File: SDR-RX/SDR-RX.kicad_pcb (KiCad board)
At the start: 2 copper layers, 43 parts, among them J1 Program, J2 Conn_01x02_Female, J3 Conn_Coaxial, J4 Conn_Coaxial, J5 Conn_01x03_Male, Q1 S8050, Q2 S8050, SW1 Reset ESP, U1 Si4734-D60-GU, U2 ESP32-WROOM-32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

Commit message: changed J2 footprint
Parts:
- J2: footprint Connector_JST:JST_XH_S2B-XH-A_1x02_P2.50mm_Horizontal -> Connector_JST:JST_XH_S2B-XH-A-1_1x02_P2.50mm_Horizontal
- moved C5 6.35 mm to (52.1, -66.0)
- moved TP1 2.54 mm to (94.0, -48.3)
- moved D4 2.54 mm to (59.7, -74.9)
- moved U3 2.54 mm to (52.1, -74.9)
- moved TP4 1.27 mm to (66.0, -48.3)
- moved C12 1.27 mm to (55.9, -66.0)
- moved C6 1.27 mm to (48.3, -66.0)
- moved SW1 1.27 mm to (94.0, -38.1)
- moved J2 1.27 mm to (50.8, -38.1)
- moved TP3 1.27 mm to (81.3, -48.3)

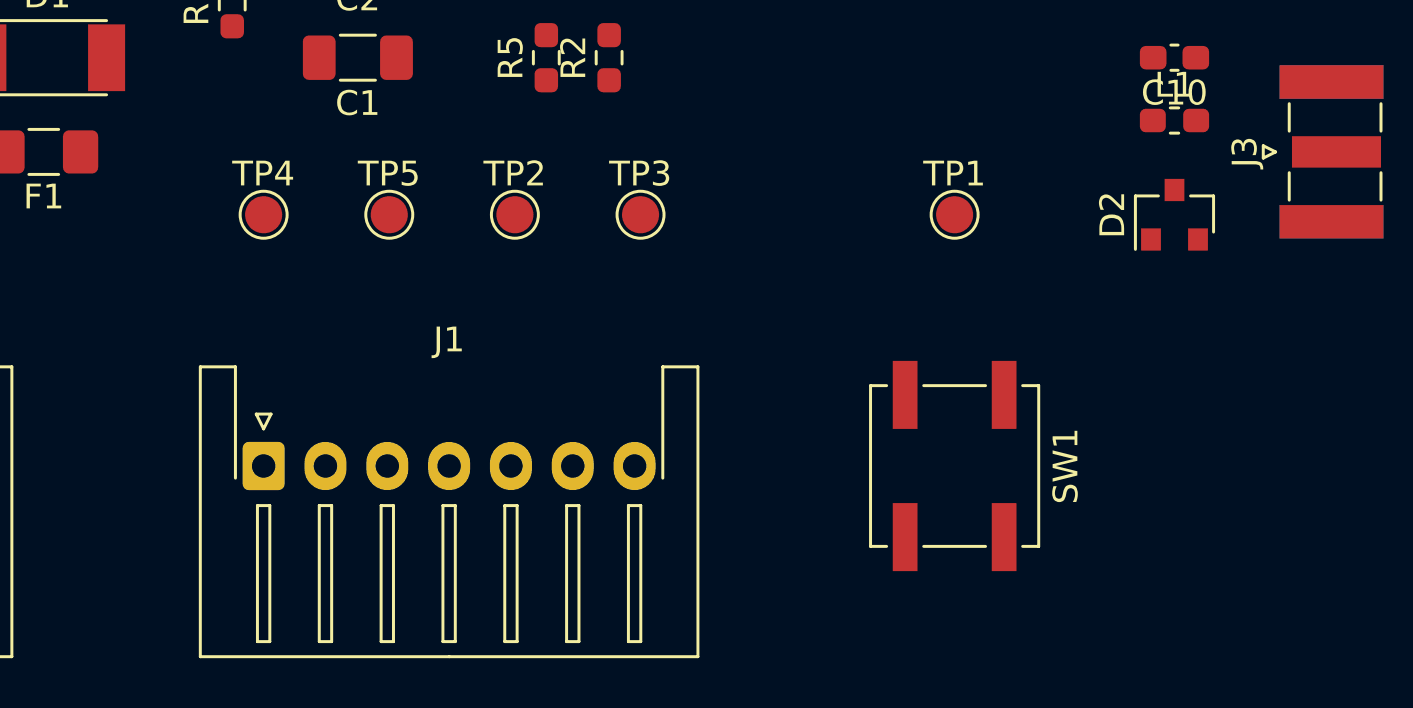
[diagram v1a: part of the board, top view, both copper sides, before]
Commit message: added SW2
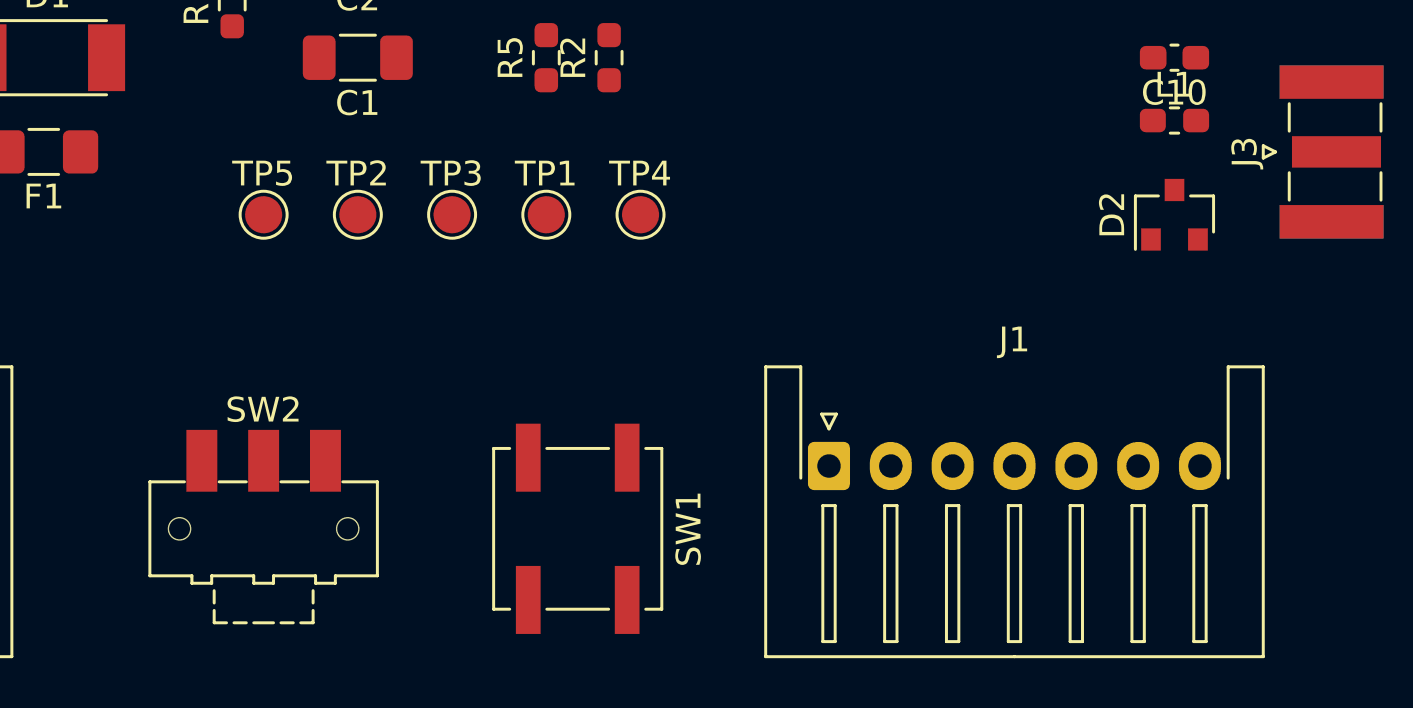
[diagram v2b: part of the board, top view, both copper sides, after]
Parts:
- added SW2: 3V3 J5/J2, Button_Switch_SMD:SW_SPDT_CK-JS102011SAQN, F.Cu at (66.0, -35.6)
- moved J1 22.9 mm to (88.9, -38.1)
- moved TP1 16.5 mm to (77.5, -48.3)
- moved SW1 15.5 mm to (78.7, -35.6)
- moved TP4 15.2 mm to (81.3, -48.3)
- moved TP3 7.62 mm to (73.7, -48.3)
- moved TP2 6.35 mm to (69.8, -48.3)
- moved TP5 5.08 mm to (66.0, -48.3)
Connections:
- C5 pad 1: +3V3 -> Net-(C5-Pad1)
- C6 pad 1: +3V3 -> Net-(C5-Pad1)
- D4 pad 2: +3V3 -> Net-(D4-Pad2)
- J1 pad 5: +3V3 -> Net-(C5-Pad1)
- U3 pad 2: +3V3 -> Net-(D4-Pad2)

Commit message: rearanged parts
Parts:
- moved Y1 14.8 mm to (92.7, -62.2)
- moved C3 14.8 mm to (87.6, -73.7)
- moved C7 14.8 mm to (97.8, -62.2), turned to 0 degrees
- moved C8 14.8 mm to (87.6, -63.5)
- moved C9 14.8 mm to (87.6, -68.6)
- moved U1 14.8 mm to (95.2, -69.8)
- moved C4 14.8 mm to (87.6, -66.0)
- moved R6 14.8 mm to (87.6, -71.1)
- moved C10 12.8 mm to (104.1, -67.3)
- moved C11 12.8 mm to (104.1, -81.3)
- moved D2 12.8 mm to (104.1, -61.0)
- moved D3 12.8 mm to (104.1, -77.5)
- moved J3 12.8 mm to (110.5, -63.5)
- moved L1 12.8 mm to (104.1, -64.8)
- moved J4 12.8 mm to (110.5, -78.7)
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
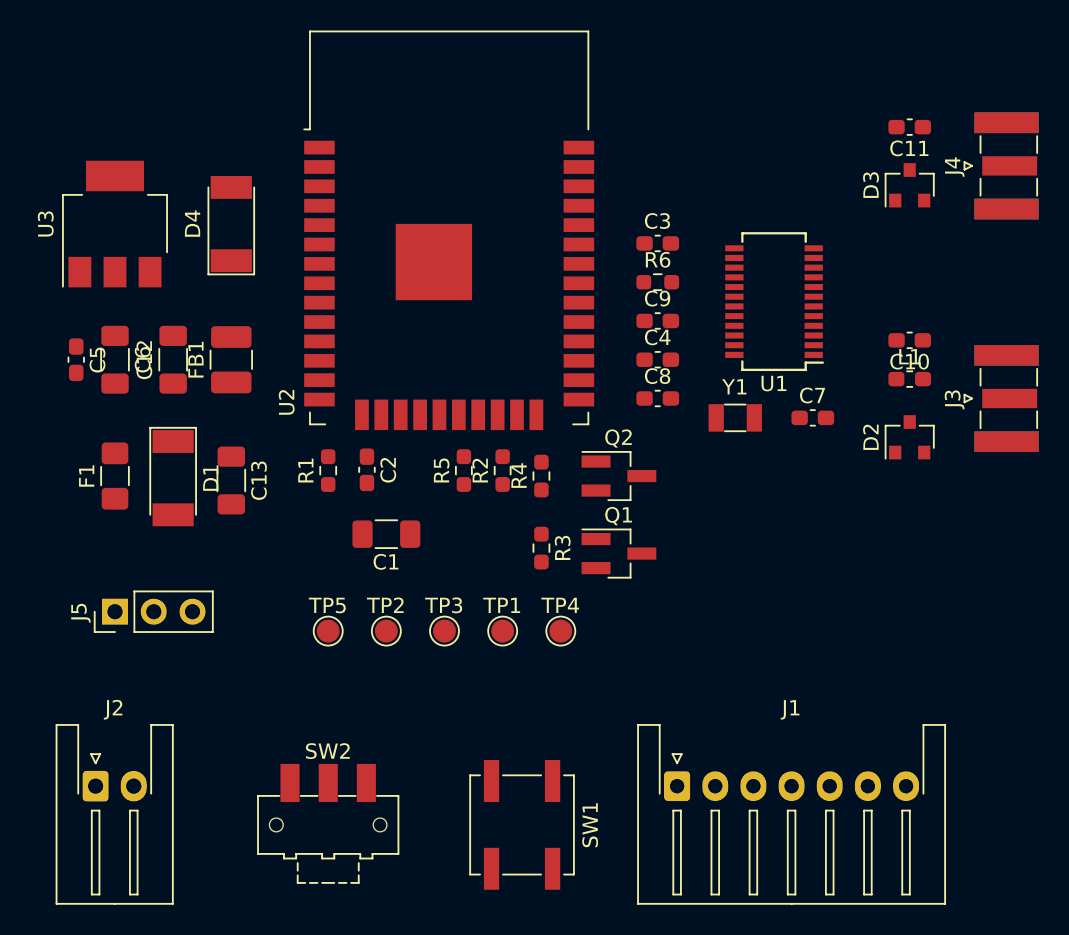
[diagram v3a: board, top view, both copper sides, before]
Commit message: put parts closer on PCB
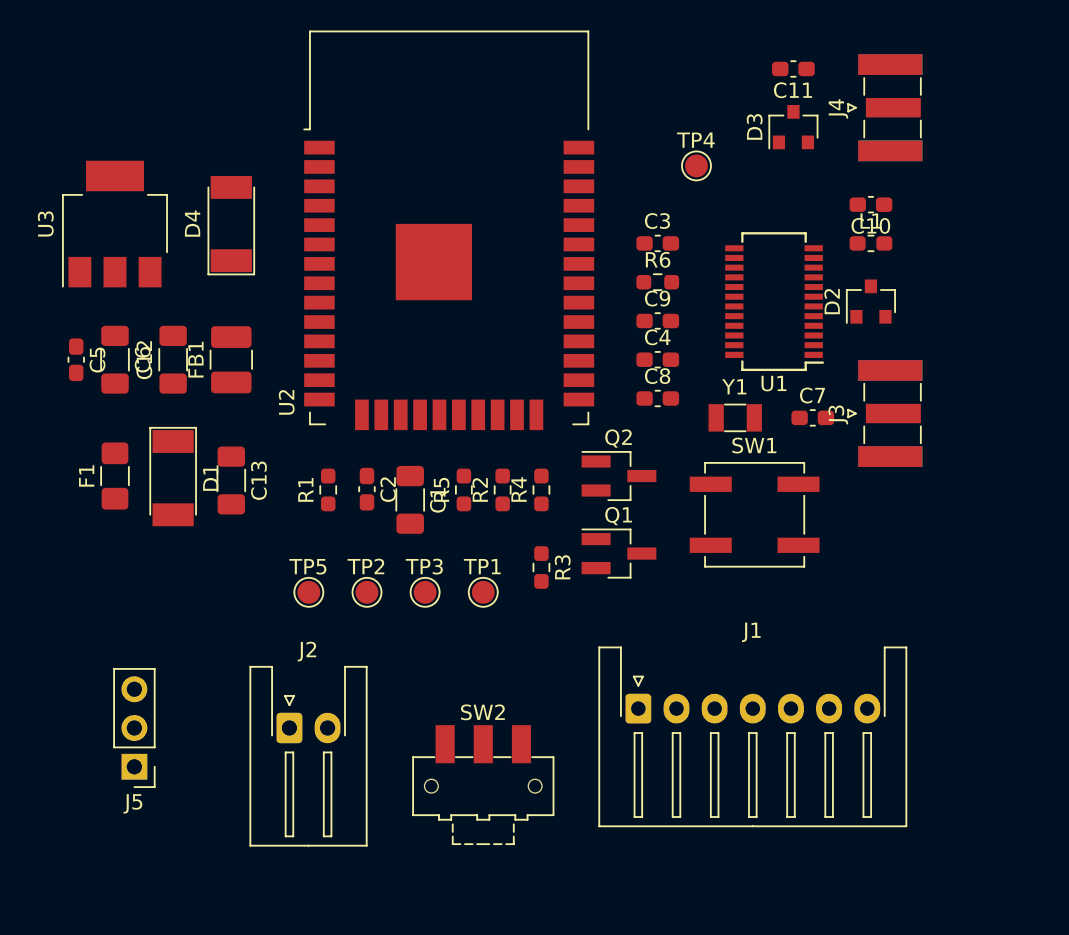
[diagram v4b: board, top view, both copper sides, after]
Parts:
- FB1: value 0Ω @ 100MHZ 1A -> 1kΩ @ 100MHz
- J2: value Conn_01x02_Female -> Vin
- J3: value Conn_Coaxial -> FM Antenna
- J4: value Conn_Coaxial -> AM Antenna
- moved TP4 31.8 mm to (90.2, -78.7)
- moved SW1 25.4 mm to (94.0, -55.9), turned to 0 degrees
- moved J2 13.3 mm to (63.5, -41.9)
- moved SW2 10.5 mm to (76.2, -38.1)
- moved J5 10.2 mm to (53.3, -39.4), turned to 180 degrees
- moved C10 9.25 mm to (101.6, -76.2)
- moved L1 9.25 mm to (101.6, -73.7)
- moved D2 9.25 mm to (101.6, -69.8)
- moved C11 8.52 mm to (96.5, -85.1)
- moved D3 8.52 mm to (96.5, -81.3)
- moved J4 8.52 mm to (102.9, -82.5)
- moved J3 7.68 mm to (102.9, -62.5)
- moved J1 5.68 mm to (86.4, -43.2)
- moved TP5 2.84 mm to (64.8, -50.8)
- moved TP1 2.84 mm to (76.2, -50.8)
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
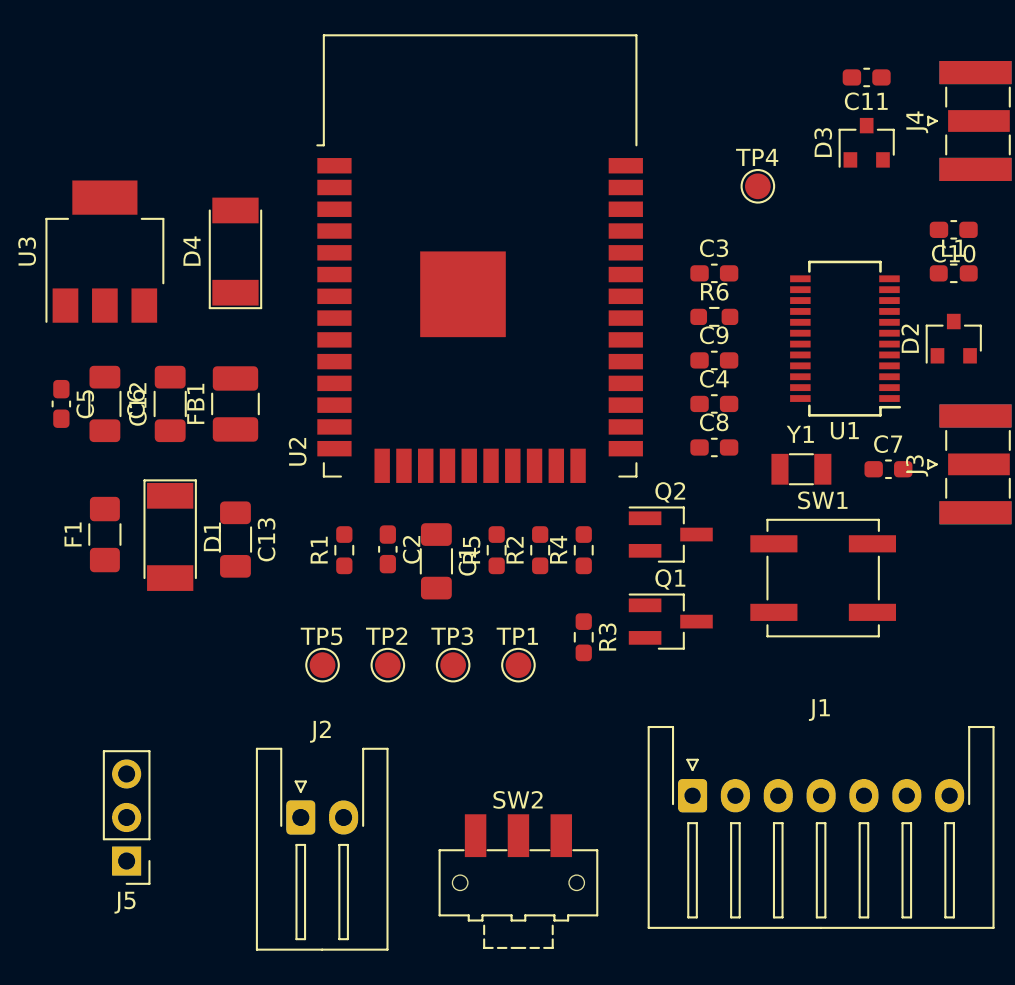
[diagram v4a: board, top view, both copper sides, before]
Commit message: rearraanged RF parts
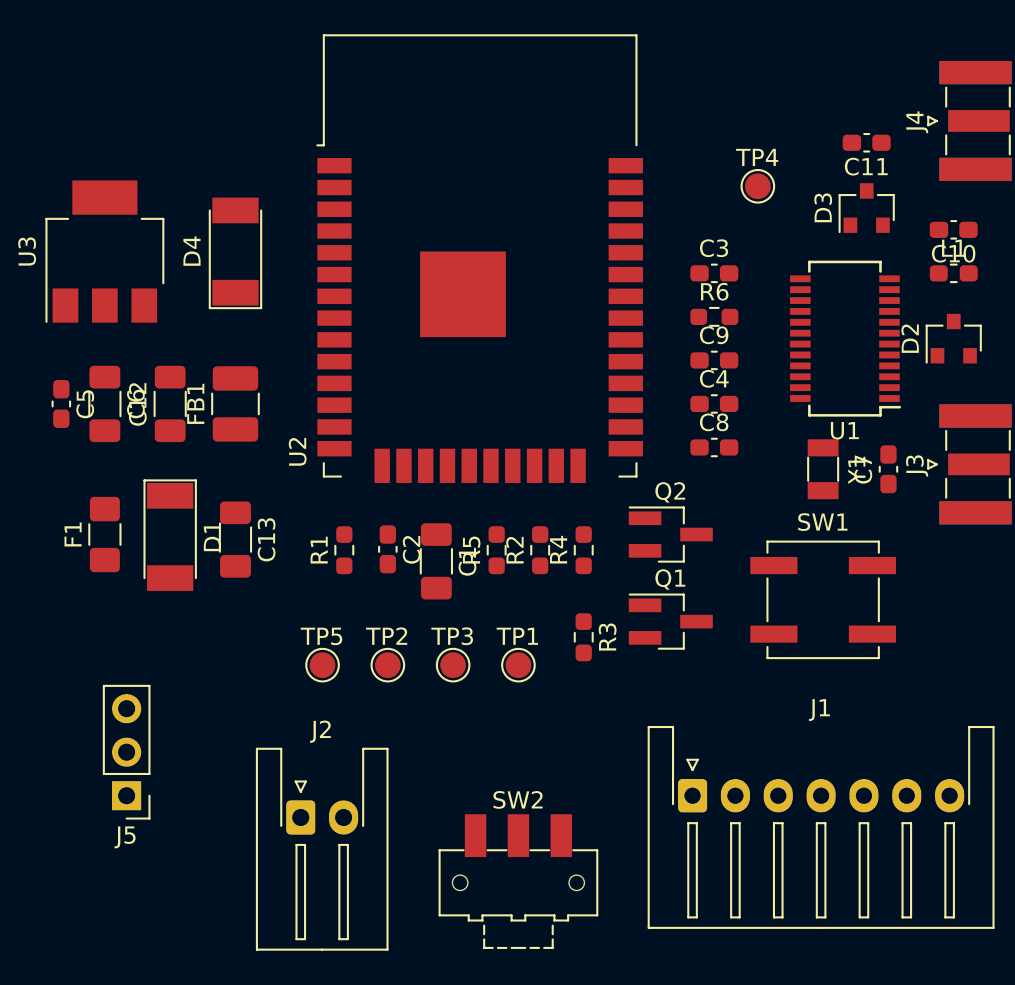
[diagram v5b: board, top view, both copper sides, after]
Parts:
- moved C11 3.81 mm to (96.5, -81.3)
- moved D3 3.81 mm to (96.5, -77.5)
- moved J5 3.81 mm to (53.3, -43.2)
- moved Y1 1.27 mm to (94.0, -62.2), turned to 270 degrees
- moved SW1 1.27 mm to (94.0, -54.6)
- turned C7 to 90 degrees
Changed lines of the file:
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@@
   )
   (module Connector_PinHeader_2.54mm:PinHeader_1x03_P2.54mm_Vertical (layer F.Cu)
-    (at 53.34 -39.37 180)
+    (at 53.34 -43.18 180)
     (descr "Through hole straight pin header, 1x03, 2.54mm pitch, single row")
     (tags "Through hole pin header THT 1x03 2.54mm single row")
@@
   )
   (module Crystal:Crystal_SMD_3215-2Pin_3.2x1.5mm (layer F.Cu)
-    (at 92.71 -62.23)
+    (at 93.98 -62.23 270)
     (descr "SMD Crystal FC-135 https://support.epson.biz/td/api/doc_check.php?dl=brief_FC-135R_en.pdf")
     (tags "SMD SMT Crystal")
     (attr smd)
-    (fp_text reference Y1 (at 0 -2) (layer F.SilkS)
-      (effects (font (size 1 1) (thickness 0.15)))
-    )
-    (fp_text value 32.768kHz (at 0 2) (layer F.Fab)
-      (effects (font (size 1 1) (thickness 0.15)))
-    )
-    (fp_text user %R (at 0 -2) (layer F.Fab)
+    (fp_text reference Y1 (at 0 -2 90) (layer F.SilkS)
+      (effects (font (size 1 1) (thickness 0.15)))
+    )
+    (fp_text value 32.768kHz (at 0 2 90) (layer F.Fab)
+      (effects (font (size 1 1) (thickness 0.15)))
+    )
+    (fp_text user %R (at 0 -2 90) (layer F.Fab)
       (effects (font (size 1 1) (thickness 0.15)))
     )
@@
     (fp_line (start -2 -1.15) (end -2 1.15) (layer F.CrtYd) (width 0.05))
     (fp_line (start 2 -1.15) (end 2 1.15) (layer F.CrtYd) (width 0.05))
-    (pad 2 smd rect (at -1.25 0) (size 1 1.8) (layers F.Cu F.Paste F.Mask)
+    (pad 2 smd rect (at -1.25 0 270) (size 1 1.8) (layers F.Cu F.Paste F.Mask)
       (net 4 "Net-(C4-Pad2)"))
-    (pad 1 smd rect (at 1.25 0) (size 1 1.8) (layers F.Cu F.Paste F.Mask)
+    (pad 1 smd rect (at 1.25 0 270) (size 1 1.8) (layers F.Cu F.Paste F.Mask)
       (net 5 "Net-(C7-Pad1)"))
     (model ${KISYS3DMOD}/Crystal.3dshapes/Crystal_SMD_3215-2Pin_3.2x1.5mm.wrl
@@
   )
   (module Button_Switch_SMD:SW_SPST_B3SL-1002P (layer F.Cu)
-    (at 93.98 -55.88)
+    (at 93.98 -54.61)
     (descr "Middle Stroke Tactile Switch, B3SL")
     (tags "Middle Stroke Tactile Switch")
@@
   )
   (module Package_TO_SOT_SMD:SOT-23 (layer F.Cu)
-    (at 96.52 -81.28 90)
+    (at 96.52 -77.47 90)
     (descr "SOT-23, Standard")
     (tags SOT-23)
@@
   )
   (module Capacitor_SMD:C_0603_1608Metric_Pad1.08x0.95mm_HandSolder (layer F.Cu)
-    (at 96.52 -85.09 180)
+    (at 96.52 -81.28 180)
     (descr "Capacitor SMD 0603 (1608 Metric), square (rectangular) end terminal, IPC_7351 nominal with elongated pad for handsoldering. (Body size source: IPC-SM-782 page 76, https://www.pcb-3d.com/wordpress/wp-content/uploads/ipc-sm-782a_amendment_1_and_2.pdf), generated with kicad-footprint-generator")
     (tags "capacitor handsolder")
@@
   )
   (module Capacitor_SMD:C_0603_1608Metric_Pad1.08x0.95mm_HandSolder (layer F.Cu)
-    (at 97.79 -62.23)
+    (at 97.79 -62.23 90)
     (descr "Capacitor SMD 0603 (1608 Metric), square (rectangular) end terminal, IPC_7351 nominal with elongated pad for handsoldering. (Body size source: IPC-SM-782 page 76, https://www.pcb-3d.com/wordpress/wp-content/uploads/ipc-sm-782a_amendment_1_and_2.pdf), generated with kicad-footprint-generator")
     (tags "capacitor handsolder")
     (attr smd)
-    (fp_text reference C7 (at 0 -1.43) (layer F.SilkS)
-      (effects (font (size 1 1) (thickness 0.15)))
-    )
-    (fp_text value 22pF (at 0 1.43) (layer F.Fab)
-      (effects (font (size 1 1) (thickness 0.15)))
-    )
-    (fp_text user %R (at 0 0) (layer F.Fab)
+    (fp_text reference C7 (at 0 -1.43 90) (layer F.SilkS)
+      (effects (font (size 1 1) (thickness 0.15)))
+    )
+    (fp_text value 22pF (at 0 1.43 90) (layer F.Fab)
+      (effects (font (size 1 1) (thickness 0.15)))
+    )
+    (fp_text user %R (at 0 0 90) (layer F.Fab)
       (effects (font (size 0.4 0.4) (thickness 0.06)))
     )
@@
     (fp_line (start 1.65 -0.73) (end 1.65 0.73) (layer F.CrtYd) (width 0.05))
     (fp_line (start 1.65 0.73) (end -1.65 0.73) (layer F.CrtYd) (width 0.05))
-    (pad 2 smd roundrect (at 0.8625 0) (size 1.075 0.95) (layers F.Cu F.Paste F.Mask) (roundrect_rratio 0.25)
-      (net 1 GND))
-    (pad 1 smd roundrect (at -0.8625 0) (size 1.075 0.95) (layers F.Cu F.Paste F.Mask) (roundrect_rratio 0.25)
+    (pad 2 smd roundrect (at 0.8625 0 90) (size 1.075 0.95) (layers F.Cu F.Paste F.Mask) (roundrect_rratio 0.25)
+      (net 1 GND))
+    (pad 1 smd roundrect (at -0.8625 0 90) (size 1.075 0.95) (layers F.Cu F.Paste F.Mask) (roundrect_rratio 0.25)
       (net 5 "Net-(C7-Pad1)"))
     (model ${KISYS3DMOD}/Capacitor_SMD.3dshapes/C_0603_1608Metric.wrl

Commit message: PCB layout for plastic enclosure
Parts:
- added H1: MountingHole_Pad, MountingHole:MountingHole_2.7mm_Pad_Via, F.Cu at (126.7, 68.2)
- added H2: MountingHole_Pad, MountingHole:MountingHole_2.7mm_Pad_Via, F.Cu at (126.7, 112.2)
- added H3: MountingHole_Pad, MountingHole:MountingHole_2.7mm_Pad_Via, F.Cu at (172.7, 112.2)
- added H4: MountingHole_Pad, MountingHole:MountingHole_2.7mm_Pad_Via, F.Cu at (172.7, 68.2)
- added J6: GPS, Connector_JST:JST_SH_BM04B-SRSS-TB_1x04-1MP_P1.00mm_Vertical, F.Cu at (165.1, 71.1)
- J2: footprint Connector_JST:JST_XH_S2B-XH-A-1_1x02_P2.50mm_Horizontal -> Connector_JST:JST_XH_B2B-XH-A_1x02_P2.50mm_Vertical
- J4: footprint Connector_Coaxial:SMA_Samtec_SMA-J-P-X-ST-EM1_EdgeMount -> Connector_Coaxial:SMB_Jack_Vertical
- moved U3 194.3 mm to (135.9, 100.3), turned to 180 degrees
- moved TP4 192.0 mm to (171.4, 95.2), turned to 270 degrees
- moved F1 190.0 mm to (146.1, 106.7), turned to 0 degrees
- moved FB1 187.8 mm to (133.3, 106.7), turned to 180 degrees
- moved TP2 187.0 mm to (171.4, 105.4), turned to 270 degrees
- moved C12 186.8 mm to (127.0, 106.7), turned to 180 degrees
- moved D4 185.8 mm to (139.7, 92.7), turned to 180 degrees
- moved C3 185.7 mm to (172.7, 91.4)
- moved J5 185.3 mm to (154.9, 111.8), turned to 90 degrees
- moved TP5 185.0 mm to (171.4, 100.3), turned to 270 degrees
- moved TP1 184.8 mm to (166.4, 110.5), turned to 270 degrees
- moved C2 184.3 mm to (165.1, 99.5), turned to 90 degrees
- moved D1 184.0 mm to (144.8, 102.9), turned to 180 degrees
- moved C13 183.2 mm to (139.7, 106.7), turned to 180 degrees
- moved TP3 182.3 mm to (166.4, 105.4), turned to 270 degrees
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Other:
- board outline added: 53 x 51 mm
